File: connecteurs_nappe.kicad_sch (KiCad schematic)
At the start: 4 parts, among them J1 NAPPE_ADC1, J2 NAPPE_ADC2, J3 NAPPE_PWM, J4 NAPPE_GPIO

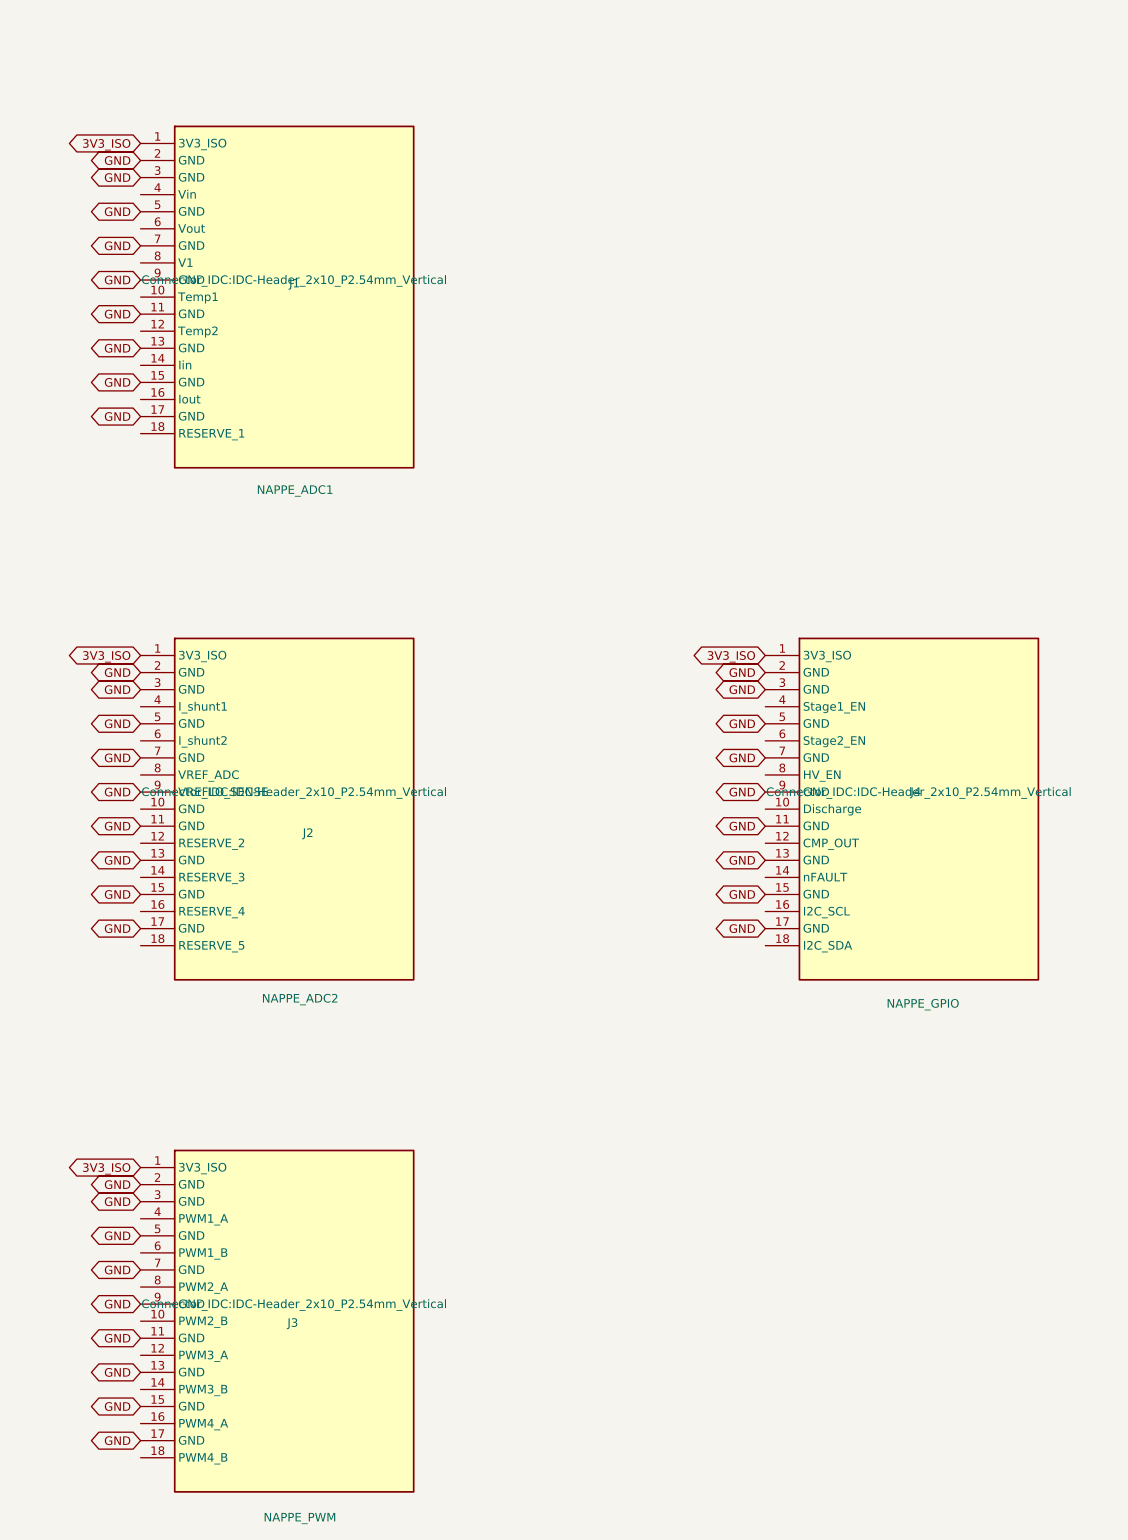
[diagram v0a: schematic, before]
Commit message: Route les nappes ADC-1/ADC-2/PWM/GPIO, ajoute GPIO-2 et COM (decision #17)
Les connecteurs J1-J4 n'avaient que leurs broches d'alimentation cablees
(3V3_ISO/GND) depuis la decision #13 - les signaux reels (Vin, PWM1_A,
Stage1_EN, etc.) n'etaient jamais poses. Cable maintenant, labels exacts
verifies par kicad-cli sch erc.

Resequencement signal(impair)/masse(pair) a partir de la broche 3 (au
lieu de masse en 2 et 3 avant le premier signal) : gagne un emplacement
signal de plus par connecteur (9 au lieu de 8) sans changer de taille de
connecteur - contrainte de stock, pas de 2x13 disponible.

Deux connecteurs neufs, meme famille 2x10 : GPIO-2 (J13, entierement en
reserve) et COM (J14, bus UART/SPI/CAN en logique 3,3V brute, les
transceivers restent sur chaque carte fille). CLB_OUT (broche devkit
orpheline) rapatrie sur GPIO-1. Bibliotheque externe
lib/C2000_Devkit_Connectors.kicad_sym synchronisee avec la copie
embarquee pour eviter lib_symbol_issues et un ecrasement silencieux par
un futur "Update Symbols from Library".

netclass_patterns (shield.kicad_pro) etendu : UART_TX/RX et CAN_TX/RX
rejoignent SPI dans la classe Rapide.

Point signale, hors perimetre : Stage1_EN/Stage2_EN/HV_EN/Discharge
restent isolated_pin_label (ERC) - ces noms viennent de l'ancien firmware
TMS320F28027, la nouvelle carte de conversion 0-500V (nouveau MCU, projet
separe) n'a pas encore choisi ses broches devkit.
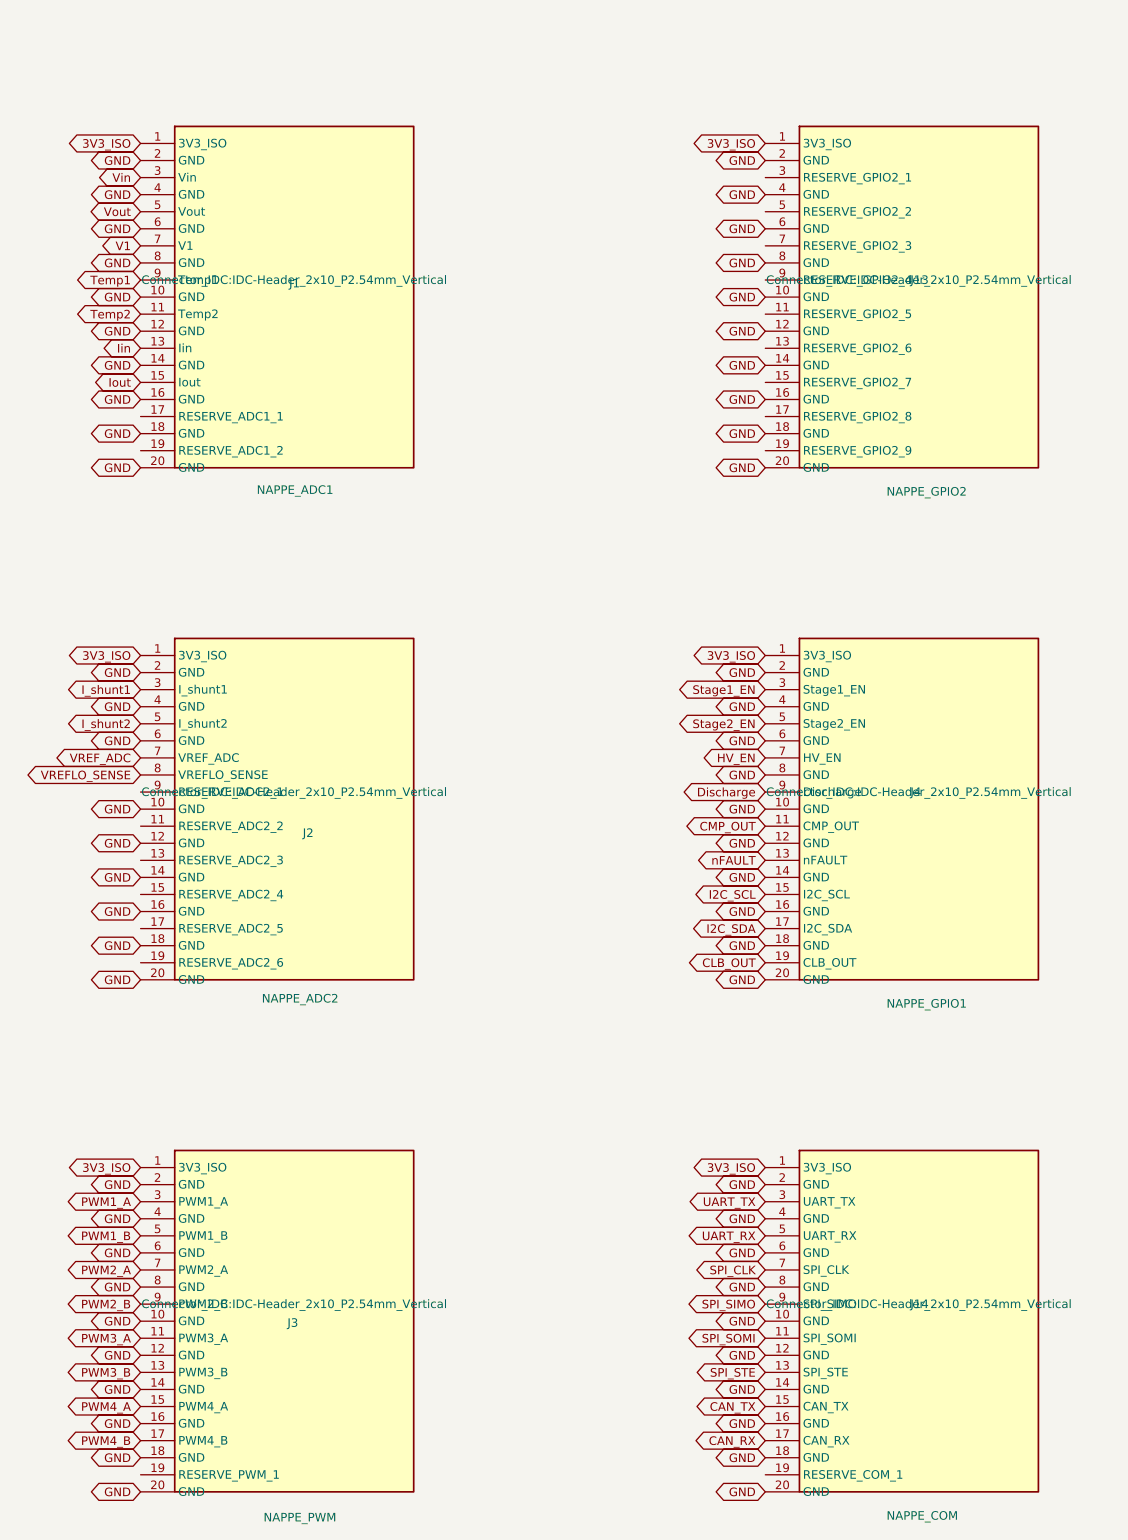
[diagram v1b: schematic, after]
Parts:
- added J13: NAPPE_GPIO2, Connector_IDC:IDC-Header_2x10_P2.54mm_Vertical, symbol C2000_Devkit_Connectors:NAPPE_GPIO2
- added J14: NAPPE_COM, Connector_IDC:IDC-Header_2x10_P2.54mm_Vertical, symbol C2000_Devkit_Connectors:NAPPE_COM
- J4: value NAPPE_GPIO -> NAPPE_GPIO1; symbol C2000_Devkit_Connectors:NAPPE_GPIO -> C2000_Devkit_Connectors:NAPPE_GPIO1
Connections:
- net 3V3_ISO: now also J13.1 (3V3_ISO), J14.1 (3V3_ISO)
- net GND: now also J1.10 (GND), J1.12 (GND), J1.14 (GND), J1.16 (GND), J1.18 (GND), J1.20 (GND), J1.4 (GND), J1.6 (GND), J1.8 (GND), J2.10 (GND), J2.12 (GND), J2.14 (GND), J2.16 (GND), J2.18 (GND), J2.20 (GND), J2.4 (GND), J2.6 (GND), J3.10 (GND), J3.12 (GND), J3.14 (GND), J3.16 (GND), J3.18 (GND), J3.20 (GND), J3.4 (GND), J3.6 (GND), J3.8 (GND), J4.10 (GND), J4.12 (GND), J4.14 (GND), J4.16 (GND), J4.18 (GND), J4.20 (GND), J4.4 (GND), J4.6 (GND), J4.8 (GND), J13.10 (GND), J13.12 (GND), J13.14 (GND), J13.16 (GND), J13.18 (GND), J13.2 (GND), J13.20 (GND), J13.4 (GND), J13.6 (GND), J13.8 (GND), J14.10 (GND), J14.12 (GND), J14.14 (GND), J14.16 (GND), J14.18 (GND), J14.2 (GND), J14.20 (GND), J14.4 (GND), J14.6 (GND), J14.8 (GND); no longer J1.11 (GND), J1.13 (GND), J1.15 (GND), J1.17 (GND), J1.3 (GND), J1.5 (GND), J1.7 (GND), J1.9 (GND), J2.11 (GND), J2.13 (GND), J2.15 (GND), J2.17 (GND), J2.3 (GND), J2.5 (GND), J2.7 (GND), J2.9 (VREFLO_SENSE), J3.11 (GND), J3.13 (GND), J3.15 (GND), J3.17 (GND), J3.3 (GND), J3.5 (GND), J3.7 (GND), J3.9 (GND), J4.11 (GND), J4.13 (GND), J4.15 (GND), J4.17 (GND), J4.3 (GND), J4.5 (GND), J4.7 (GND), J4.9 (GND)
- net VREFLO_SENSE: now reaches J2.8 (VREFLO_SENSE)
- new net CAN_RX: J14.17 (CAN_RX)
- new net CAN_TX: J14.15 (CAN_TX)
- new net CLB_OUT: J4.19 (CLB_OUT)
- new net CMP_OUT: J4.11 (CMP_OUT)
- new net Discharge: J4.9 (Discharge)
- new net HV_EN: J4.7 (HV_EN)
- new net I2C_SCL: J4.15 (I2C_SCL)
- new net I2C_SDA: J4.17 (I2C_SDA)
- new net I_shunt1: J2.3 (I_shunt1)
- new net I_shunt2: J2.5 (I_shunt2)
- new net Iin: J1.13 (Iin)
- new net Iout: J1.15 (Iout)
- new net PWM1_A: J3.3 (PWM1_A)
- new net PWM1_B: J3.5 (PWM1_B)
- new net PWM2_A: J3.7 (PWM2_A)
- new net PWM2_B: J3.9 (PWM2_B)
- new net PWM3_A: J3.11 (PWM3_A)
- new net PWM3_B: J3.13 (PWM3_B)
- new net PWM4_A: J3.15 (PWM4_A)
- new net PWM4_B: J3.17 (PWM4_B)
- new net SPI_CLK: J14.7 (SPI_CLK)
- new net SPI_SIMO: J14.9 (SPI_SIMO)
- new net SPI_SOMI: J14.11 (SPI_SOMI)
- new net SPI_STE: J14.13 (SPI_STE)
- new net Stage1_EN: J4.3 (Stage1_EN)
- new net Stage2_EN: J4.5 (Stage2_EN)
- new net Temp1: J1.9 (Temp1)
- new net Temp2: J1.11 (Temp2)
- new net UART_RX: J14.5 (UART_RX)
- new net UART_TX: J14.3 (UART_TX)
- new net V1: J1.7 (V1)
- new net VREF_ADC: J2.7 (VREF_ADC)
- new net Vin: J1.3 (Vin)
- new net Vout: J1.5 (Vout)
- new net nFAULT: J4.13 (nFAULT)

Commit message: Decouplage 100nF sur les 6 nappes (3V3_ISO/GND)
Un condensateur par connecteur (C29, C30, C34, C35, C42, C43), au plus
pres de chaque embase - complement du decouplage par IC deja en place,
pour que chaque nappe ait sa propre reserve locale avant la traversee du
cable. Place manuellement par l'utilisateur dans l'editeur KiCad.
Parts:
- added C29, C30, C34, C35, C42, C43: 100nF, Capacitor_SMD:C_0805_2012Metric, symbol Device:C
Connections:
- net 3V3_ISO: now also C29.1, C30.1, C34.1, C35.1, C42.1, C43.1
- net GND: now also C29.2, C30.2, C34.2, C35.2, C42.2, C43.2

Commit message: Corrige ADC-2 (I_SHUNT1_CMP/I_SHUNT2_CMP) et protege 11 signaux nappe (decisions #18-19)
ADC-2 ne cablait que la voie filtree (I_shunt1/I_shunt2) et oubliait le
chemin direct comparateur que la decision #4 impose. Ajoute en
consommant 2 des 6 reserves, sans adjacence avec la voie filtree (les
deux chemins doivent rester independants).

11 signaux cables en decision #17 n'avaient aucune protection
(CLB_OUT, UART_TX/RX, SPI_CLK/SIMO/SOMI/STE, CAN_TX/RX, et les deux
I_SHUNT*_CMP une fois ajoutes) alors que les 23 autres signaux du
connecteur devkit en ont une. Nouvelle feuille protection_nappe.kicad_sch,
11 trios copies depuis un trio reel (protection_devkit3.kicad_sch) plutot
que redessines - BAT54S + R + 100pF, R=100R standard sauf les deux
I_SHUNT*_CMP a 22R (decision #4 : Rs<=50 Ohm sur ce chemin, 100R le
depasserait).

9 labels renommes en _MCU cote connecteur_devkit.kicad_sch (meme
convention que les 23 trios existants : le nom brut cote nappe, le nom
_MCU cote connecteur devkit, jamais l'inverse).

Egalement loggee : decision #18, le decoupage 100nF des 6 nappes pose
manuellement par l'utilisateur dans une session precedente.

Verifie par kicad-cli sch erc, compare par type de violation : les 11
isolated_pin_label vises ont disparu, aucune autre categorie n'augmente
sauf endpoint_off_grid (+33, un par composant neuf, meme defaut
pre-existant que les 23 trios deja en place).
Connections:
- net I_SHUNT2_CMP: now reaches J2.11 (I_SHUNT2_CMP)
- net I_SHUNT1_CMP: now reaches J2.9 (I_SHUNT1_CMP)
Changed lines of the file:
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@@
+		)
+	)
+	(global_label "I_SHUNT1_CMP"
+		(shape bidirectional)
+		(at 108.966 131.572 180)
+		(fields_autoplaced yes)
+		(effects
+			(font
+				(size 1.27 1.27)
+			)
+			(justify right)
+		)
+		(property "Intersheetrefs" "${INTERSHEET_REFS}"
+			(at 108.966 131.572 0)
+			(hide yes)
+			(show_name no)
+			(do_not_autoplace no)
+			(effects
+				(font
+					(size 1.27 1.27)
+				)
+			)
+		)
+	)
+	(global_label "I_SHUNT2_CMP"
+		(shape bidirectional)
+		(at 108.966 136.652 180)
+		(fields_autoplaced yes)
+		(effects
+			(font
+				(size 1.27 1.27)
+			)
+			(justify right)
+		)
+		(property "Intersheetrefs" "${INTERSHEET_REFS}"
+			(at 108.966 136.652 0)
+			(hide yes)
+			(show_name no)
+			(do_not_autoplace no)
+			(effects
+				(font
+					(size 1.27 1.27)
+				)
+			)
 		)
 	)

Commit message: Deplace I_SHUNT1_CMP/I_SHUNT2_CMP d'ADC-2, positions 9/11 -> 11/13
Position 9 etait adjacente a VREFLO_SENSE (position 8, deja hors de
l'alternance stricte signal/masse en tant que paire de reference) sans
masse entre les deux. Un signal inutilise (reserve) a cet endroit etait
inoffensif ; I_SHUNT1_CMP (classe Rapide, comparateur, edges rapides)
ne l'est pas - meme defaut de blindage que partout ailleurs sur ce
connecteur. Deplace en 11/13, entourees de masse des deux cotes, comme
I_shunt1/I_shunt2 en 3/5. Position 9 redevient reserve ADC2-1.

ERC : memes categories/comptes qu'avant (34 pin_not_connected), pin 9
desormais signale non connecte (attendu, reserve), pins 11/13 ne le
sont plus plus. Necessite un nouveau "Update PCB from Schematic" (le
numero de broche physique du pad concerne change sur ADC-2).
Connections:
- net I_SHUNT1_CMP: now also J2.11 (I_SHUNT1_CMP); no longer J2.9 (I_SHUNT1_CMP)
- net I_SHUNT2_CMP: now also J2.13 (I_SHUNT2_CMP); no longer J2.11 (I_SHUNT2_CMP)
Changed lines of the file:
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@@
 	(global_label "I_SHUNT1_CMP"
-		(shape bidirectional)
-		(at 108.966 131.572 180)
-		(fields_autoplaced yes)
-		(effects
-			(font
-				(size 1.27 1.27)
-			)
-			(justify right)
-		)
-		(property "Intersheetrefs" "${INTERSHEET_REFS}"
-			(at 108.966 131.572 0)
-			(hide yes)
-			(show_name no)
-			(do_not_autoplace no)
-			(effects
-				(font
-					(size 1.27 1.27)
-				)
-			)
-		)
-	)
-	(global_label "I_SHUNT2_CMP"
 		(shape bidirectional)
 		(at 108.966 136.652 180)
@@
 			(hide yes)
 			(show_name no)
+			(do_not_autoplace no)
+			(effects
+				(font
+					(size 1.27 1.27)
+				)
+			)
+		)
+	)
+	(global_label "I_SHUNT2_CMP"
+		(shape bidirectional)
+		(at 108.966 141.732 180)
+		(fields_autoplaced yes)
+		(effects
+			(font
+				(size 1.27 1.27)
+			)
+			(justify right)
+		)
+		(property "Intersheetrefs" "${INTERSHEET_REFS}"
+			(at 108.966 141.732 0)
+			(hide yes)
+			(show_name no)

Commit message: Supprime l'exception d'adjacence 7/8 sur ADC-2, alternance stricte partout
Correction precedente insuffisante : deplacer seulement I_SHUNT1_CMP/
I_SHUNT2_CMP (9/11 -> 11/13) laissait VREF_ADC/VREFLO_SENSE adjacents
en 7/8 sans masse entre eux - une exception qui n'a plus lieu d'etre
puisque leur lien electrique passe par le suiveur rail-to-rail du
shield, pas par leur proximite sur la nappe.

Nouveau brochage ADC-2, alternance stricte masse/signal, zero exception :
  3 VREFLO_SENSE, 5 VREF_ADC (etaient 7/8)
  7 I_shunt1, 9 I_shunt2 (etaient 3/5)
  11 I_SHUNT1_CMP, 13 I_SHUNT2_CMP (inchange)
  15/17/19 reserves (renumerotees 1-3, une reserve perdue dans l'echange)

ERC : pin_not_connected 34->33 (une reserve en moins), aucune
regression. Necessite Update PCB from Schematic + re-routage manuel
des pistes I_shunt1/I_shunt2 deja posees (le changement de net sur un
pad existant ne deplace pas la piste vers le nouveau pad).
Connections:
- net GND: now also J2.8 (GND)
- net I_shunt1: now also J2.7 (I_shunt1); no longer J2.3 (I_shunt1)
- net I_shunt2: now also J2.9 (I_shunt2); no longer J2.5 (I_shunt2)
- net VREFLO_SENSE: now also J2.3 (VREFLO_SENSE); no longer J2.8 (VREFLO_SENSE)
- net VREF_ADC: now also J2.5 (VREF_ADC); no longer J2.7 (VREF_ADC)
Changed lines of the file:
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@@
 	(global_label "VREF_ADC"
 		(shape bidirectional)
-		(at 108.966 126.492 180)
-		(fields_autoplaced yes)
-		(effects
-			(font
-				(size 1.27 1.27)
-			)
-			(justify right)
-		)
-		(property "Intersheetrefs" "${INTERSHEET_REFS}"
-			(at 108.966 126.492 0)
+		(at 108.966 121.412 180)
+		(fields_autoplaced yes)
+		(effects
+			(font
+				(size 1.27 1.27)
+			)
+			(justify right)
+		)
+		(property "Intersheetrefs" "${INTERSHEET_REFS}"
+			(at 108.966 121.412 0)
 			(hide yes)
 			(show_name no)
@@
 	(global_label "I_shunt2"
 		(shape bidirectional)
-		(at 108.966 121.412 180)
-		(fields_autoplaced yes)
-		(effects
-			(font
-				(size 1.27 1.27)
-			)
-			(justify right)
-		)
-		(property "Intersheetrefs" "${INTERSHEET_REFS}"
-			(at 108.966 121.412 0)
+		(at 108.966 131.572 180)
+		(fields_autoplaced yes)
+		(effects
+			(font
+				(size 1.27 1.27)
+			)
+			(justify right)
+		)
+		(property "Intersheetrefs" "${INTERSHEET_REFS}"
+			(at 108.966 131.572 0)
 			(hide yes)
 			(show_name no)
@@
 	(global_label "VREFLO_SENSE"
 		(shape bidirectional)
+		(at 108.966 116.332 180)
+		(fields_autoplaced yes)
+		(effects
+			(font
+				(size 1.27 1.27)
+			)
+			(justify right)
+		)
+		(property "Intersheetrefs" "${INTERSHEET_REFS}"
+			(at 108.966 116.332 0)
+			(hide yes)
+			(show_name no)
+			(do_not_autoplace no)
+			(effects
+				(font
+					(size 1.27 1.27)
+				)
+			)
+		)
+	)
+	(global_label "GND"
+		(shape bidirectional)
 		(at 108.966 129.032 180)
 		(fields_autoplaced yes)
@@
 	(global_label "I_shunt1"
 		(shape bidirectional)
-		(at 108.966 116.332 180)
-		(fields_autoplaced yes)
-		(effects
-			(font
-				(size 1.27 1.27)
-			)
-			(justify right)
-		)
-		(property "Intersheetrefs" "${INTERSHEET_REFS}"
-			(at 108.966 116.332 0)
-			(hide yes)
-			(show_name no)
+		(at 108.966 126.492 180)
+		(fields_autoplaced yes)
+		(effects
+			(font
+				(size 1.27 1.27)
+			)
+			(justify right)
+		)
+		(property "Intersheetrefs" "${INTERSHEET_REFS}"
+			(at 108.966 126.492 0)
+			(hide yes)
+			(show_name no)

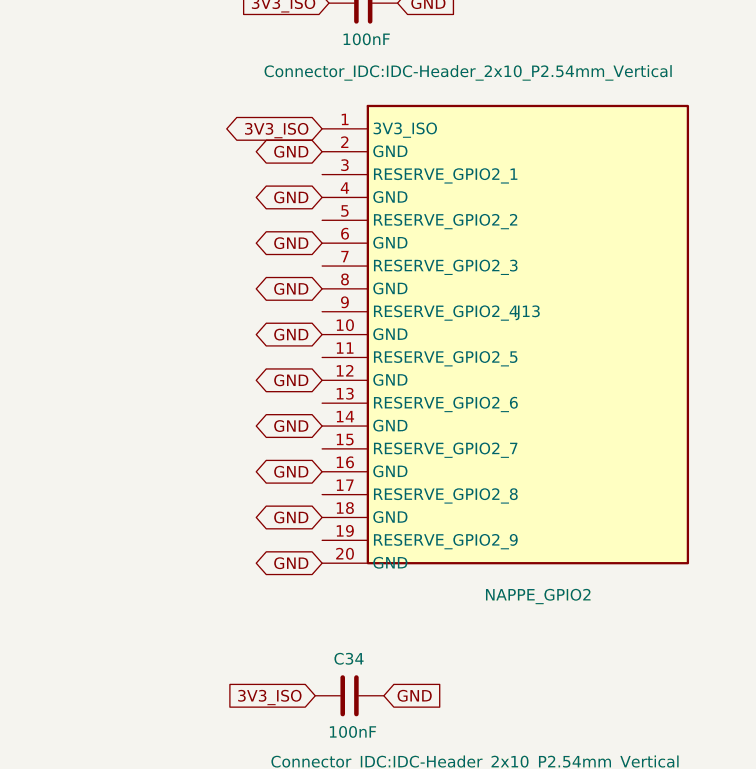
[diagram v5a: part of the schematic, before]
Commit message: CLB du F28P551 en mini-CPLD : report devkit, 4 trios, nappe logic (decision #20)
- Report sur connecteur_devkit.kicad_sch (symboles + labels reels, lib
  externe incluse) du reseequencement devkit (Iin/Iout/V1/Temp1/Temp2/
  ADC_8-12/I_SHUNT*_CMP/I_SHUNT*_MES deplaces) et des 4 broches neuves
  (Stage1_EN=GPIO9, Stage2_EN=GPIO20, HV_EN=GPIO21, Discharge=GPIO41).
- Corrige un erratum trouve en verifiant : protection_devkit3.kicad_sch
  gardait l'ancien nom nFAULT_MCU apres le renommage du connecteur en
  ~{FAULT_MCU}, coupant silencieusement le trio existant (meme categorie
  de bug que l'erratum ADC-2 de la decision #19).
- 4 nouveaux trios de protection D36-39/R35-38/C55-58, R=10R (signaux
  classes Rapide, decision explicite), pour les 4 sorties neuves.
- Nappe GPIO-2 renommee nappe "logic" (NAPPE_LOGIC, J13) : 9 reserves
  deviennent CLB_Out_1-4/CLB_In_1-5 (noms cosmetiques sur le connecteur
  uniquement, le net electrique reste le vrai nom de signal). 4 sorties
  protegees + 5 entrees tapees sans sacrifice (CAN_RX/CAN_TX, PWM2_B/
  PWM3_B/PWM4_B - deja protegees ailleurs, lues en plus ici).
- netclass_patterns, used_designators, doc/decisions.md #20,
  doc/nappes-shield.md, doc/brochage-devkit.csv mis a jour.

ERC : isolated_pin_label 9->5 (reste les 5 reserves ADC libres, hors
perimetre), pin_not_connected -9 (nappe logic cablee), aucune nouvelle
categorie.
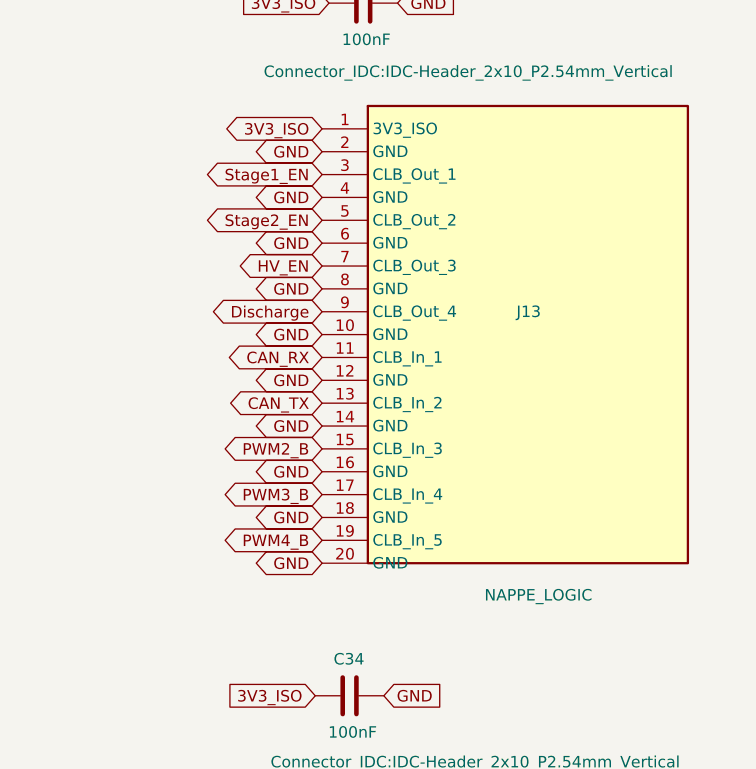
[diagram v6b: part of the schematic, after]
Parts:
- J13: value NAPPE_GPIO2 -> NAPPE_LOGIC
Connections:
- net CAN_RX: now also J13.11 (CLB_In_1)
- net CAN_TX: now also J13.13 (CLB_In_2)
- net Discharge: now also J13.9 (CLB_Out_4)
- net HV_EN: now also J13.7 (CLB_Out_3)
- net PWM2_B: now also J13.15 (CLB_In_3)
- net PWM3_B: now also J13.17 (CLB_In_4)
- net PWM4_B: now also J13.19 (CLB_In_5)
- net Stage1_EN: now also J13.3 (CLB_Out_1)
- net Stage2_EN: now also J13.5 (CLB_Out_2)
